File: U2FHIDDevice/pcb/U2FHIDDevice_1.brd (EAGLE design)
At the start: 45.7 x 22.9 mm, 32 parts, among them CN1 TE-1734028, CN2 IF_7PIN, SW1 SKRPACE010, U1 STM32F411RET6_, U2 LD39050PU33R_DEV, U3 USBLC6-2SC6, X1 NX3215SA_

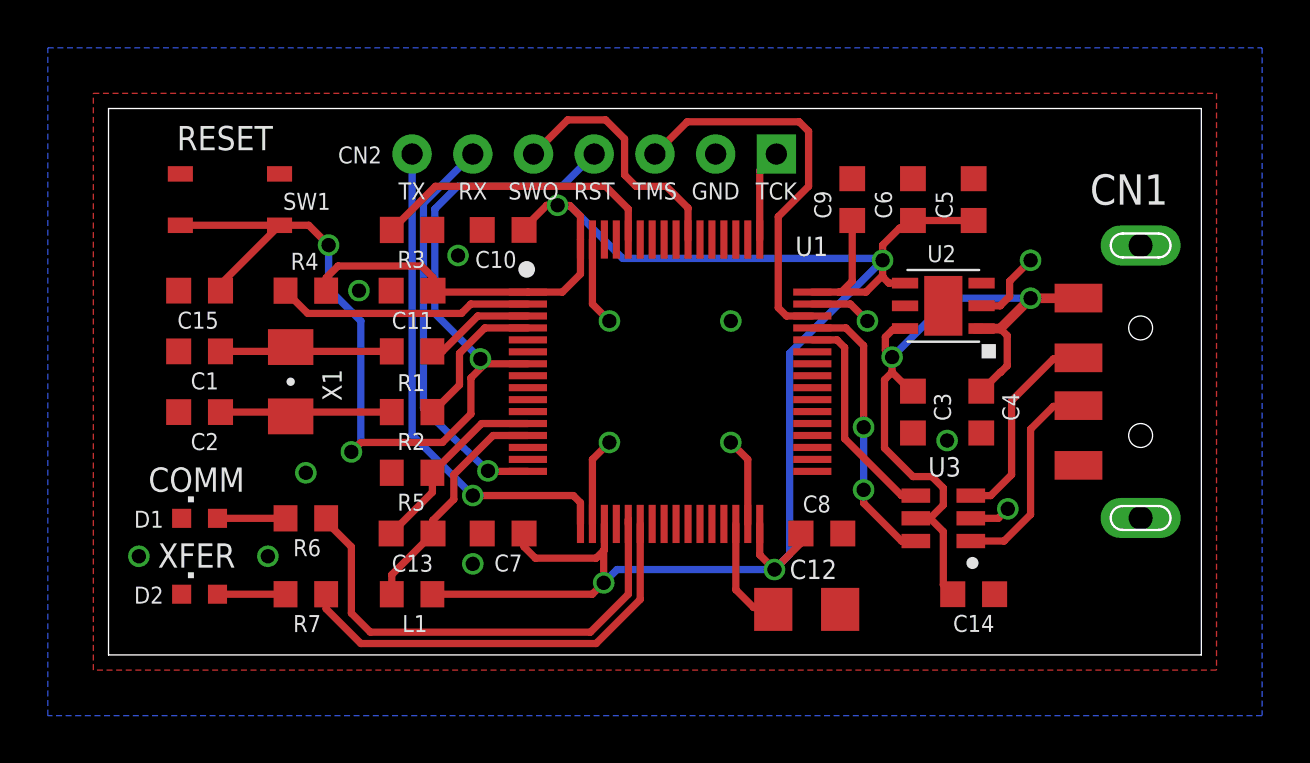
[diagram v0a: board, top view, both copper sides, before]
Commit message: 回路修正
・8MHzクリスタルを追加
・それに伴い、基板レイアウトを大幅に修正
（部品が大きく、前回レイアウトがベースだと配置できないための措置）
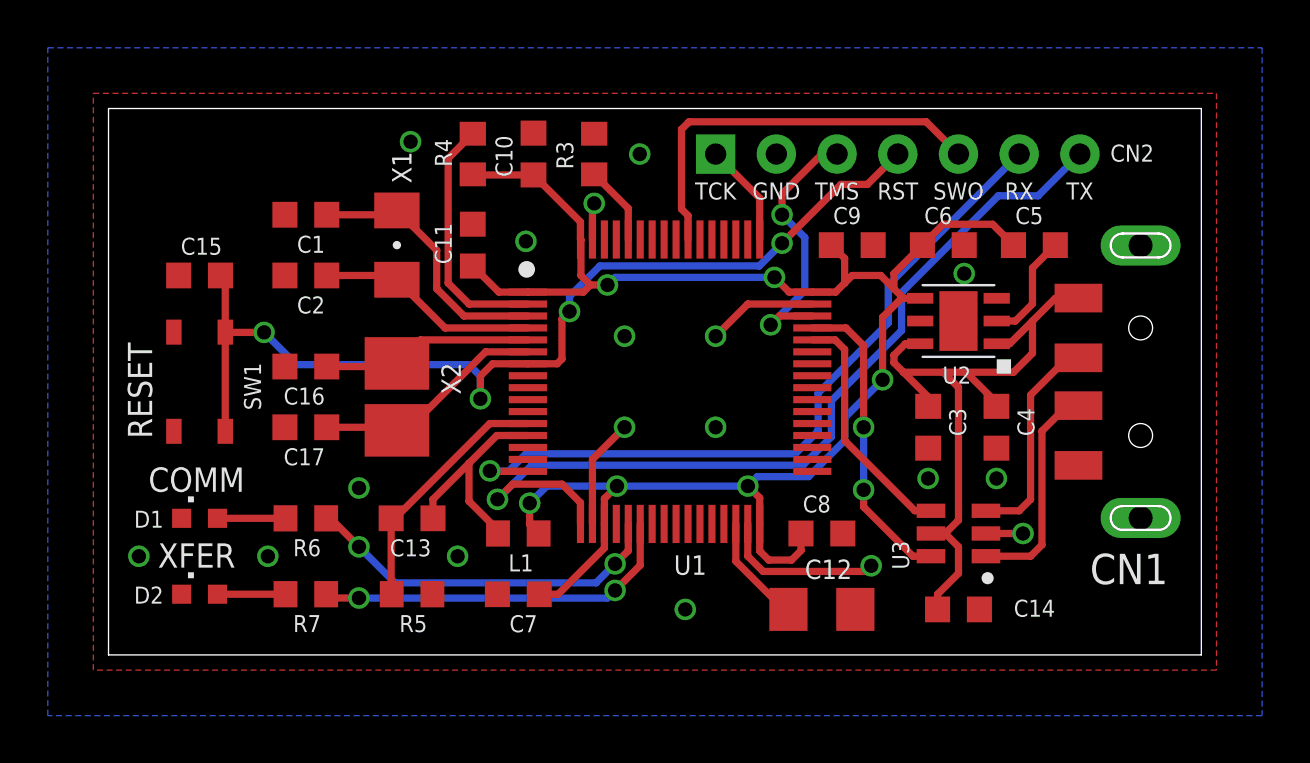
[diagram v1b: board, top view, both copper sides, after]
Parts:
- removed R1, R2: 0, Parts:R0603
- added C16, C17: 4.3pF, Parts:C0603K
- added X2: NX3225GD_, Parts:NX3225_DEV
- moved R4 9.03 mm to (15.2, 21.0), turned to 270 degrees
- moved R3 8.26 mm to (20.3, 21.0), turned to 90 degrees
- moved SW1 7.73 mm to (3.81, 11.4), turned to 270 degrees
- moved C1 7.24 mm to (8.26, 18.4)
- moved C2 7.24 mm to (8.26, 15.9)
- moved X1 7.24 mm to (12.1, 17.1)
- moved L1 5.12 mm to (17.1, 5.08)
- moved R5 5.08 mm to (12.7, 2.54), turned to 180 degrees
- moved C10 3.42 mm to (17.8, 21.0), turned to 90 degrees
- moved C5 3.18 mm to (38.7, 17.1), turned to 0 degrees
- moved C11 3.17 mm to (15.2, 17.1), turned to 90 degrees
- moved C7 2.62 mm to (17.1, 2.54)
- moved CN2 2.54 mm to (25.4, 21.0), turned to 0 degrees
- moved C6 2.29 mm to (34.9, 17.1), turned to 0 degrees
- moved C9 1.91 mm to (31.1, 17.1), turned to 0 degrees
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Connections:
- removed net N$2: C1.1, R1.1, X1.1
- removed net N$3: C2.1, R2.1, X1.2
- new net OSC_IN: C16.1, U1.5, X2.1
- new net OSC_OUT: C17.1, U1.6, X2.2
- net 0V: now also C16.2, C17.2
- net OSC32_IN: now also C1.1, X1.1; no longer R1.2
- net OSC32_OUT: now also C2.1, X1.2; no longer R2.2
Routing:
- net USART_RX: track 20.9 -> 37.1 mm
- net USART_TX: track 16.9 -> 31.4 mm
- net VDD: track 85.9 -> 71.9 mm, vias 4 -> 6
- net OSC_OUT: track 0.00 -> 9.83 mm
- net BOOT0: track 12.3 -> 3.32 mm
- net OSC_IN: track 0.00 -> 8.88 mm
- net N$2: track 7.40 -> 0.00 mm
- net N$3: track 7.40 -> 0.00 mm
- net OSC32_IN: track 4.61 -> 11.3 mm
- net SWO: track 10.8 -> 17.0 mm
- net TMS: track 16.6 -> 11.4 mm, vias 0 -> 2
- net 0V: track 18.8 -> 23.8 mm, vias 14 -> 18
- net LED_GREEN: track 20.3 -> 15.4 mm, vias 0 -> 2
- net OSC32_OUT: track 6.23 -> 9.32 mm
- net LED_BLUE: track 18.3 -> 15.5 mm, vias 0 -> 2
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
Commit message: 基板レイアウト修正
・ユーザースイッチを追加（回路はNUCLEOが参考）
・ST-LINK V2-1インターフェースピンのレイアウトが逆だったので修正
・基板サイズは修正なし
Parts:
- removed R7: 680, Parts:R0603
- added C18: 0.1uF, Parts:C0603K
- added R1: 10k, Parts:R0603
- added R2: 4.7k, Parts:R0603
- added SW2: SKRPACE010, Parts:SKRPACE010
- C11: value 1uF -> 0.1uF
- C12: value 4.7uF -> 0.1uF; device Parts:C1206 -> Parts:C0603K
- C13, C7: value 0.1uF -> 1uF
- C14: value 0.1uF -> 4.7uF; device Parts:C0603K -> Parts:C1206
- C16, C17: value 4.3pF -> 0.1uF
- C3: value 1uF -> 4.3pF
- C4: value 0.1uF -> 4.3pF
- R3: value 10k -> 0
- R4: value 10k -> 1k
- R5: value 0 -> 680
- R6: value 1k -> 100
- moved C16 29.1 mm to (35.6, 1.91), turned to 0 degrees
- moved C4 28.9 mm to (8.26, 8.26), turned to 180 degrees
- moved C7 26.1 mm to (38.7, 17.1), turned to 0 degrees
- moved C3 26.1 mm to (8.26, 10.8), turned to 180 degrees
- moved C12 21.6 mm to (19.7, 21.0), turned to 90 degrees
- moved C9 20.2 mm to (17.1, 2.54), turned to 180 degrees
- moved C10 19.9 mm to (29.8, 5.08), turned to 0 degrees
- moved R3 19.9 mm to (12.7, 2.54), turned to 180 degrees
- moved R4 16.8 mm to (8.26, 5.71), turned to 180 degrees
- moved C11 15.9 mm to (31.1, 17.1), turned to 0 degrees
- moved R6 15.7 mm to (12.1, 21.0), turned to 0 degrees
- moved C15 13.5 mm to (12.7, 5.71)
- moved C8 13.1 mm to (34.9, 17.1)
- moved C13 11.7 mm to (15.2, 17.1), turned to 90 degrees
- moved C5 8.82 mm to (34.3, 9.53), turned to 270 degrees
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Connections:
- new net N$2: C18.2, R6.1
- net 0V: now also C13.2, R1.2, R3.1, R6.2, SW2.3, SW2.4; no longer C15.2, R3.2, R5.1
- net AGND: now also C15.2, R3.2; no longer C13.2, R5.2
- net AVDD: now also C15.1; no longer C13.1
- net BOOT0: now also R1.1; no longer R3.1
- net LED_BLUE: now also R5.1; no longer R7.1
- net LED_GREEN: now also R4.1; no longer R6.1
- net N$1: now also R4.2; no longer R6.2
- net N$4: now also R5.2; no longer R7.2
- net NRST: now also C17.1; no longer C15.1
- net OSC_IN: now also C3.1; no longer C16.1
- net OSC_OUT: now also C4.1; no longer C17.1
- net U5V: now also C16.1, C5.1, C6.1; no longer C14.1, C3.1, C4.1
- net USER_BUTTON: now also C18.1, R2.1, SW2.1, SW2.2; no longer R4.1
- net VCAP_1: now also C14.1; no longer C12.1
- net VDD: now also C12.1, C13.1, R2.2; no longer C5.1, C6.1, R4.2
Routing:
- net USER_BUTTON: track 10.4 -> 31.4 mm
- net NRST: track 42.6 -> 45.2 mm
- net N$2: track 0.00 -> 2.08 mm
- net OSC_IN: track 8.88 -> 9.40 mm
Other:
- board text added: "USER"
